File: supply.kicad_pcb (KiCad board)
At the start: 2 copper layers, 70 x 54.5 mm, 27 parts, among them J1 out, J2 2, J3 3, J4 1, J5 GND, J6 Conn_01x01_Female, J7 Conn_01x01_Female, J8 Conn_01x01_Female, J9 Conn_01x01_Female, U1 TPS61040DBV

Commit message: Add files via upload
updated
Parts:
- removed D3: SB140-E3/54, Diode_THT:D_DO-41_SOD81_P7.62mm_Horizontal
- added C10: 100nF, Capacitor_THT:C_Disc_D3.8mm_W2.6mm_P2.50mm, F.Cu at (94.5, 128.0)
- added C8: 10nF, Capacitor_THT:C_Disc_D3.8mm_W2.6mm_P2.50mm, F.Cu at (59.0, 120.5)
- added C9: 1nF, Capacitor_THT:C_Disc_D3.8mm_W2.6mm_P2.50mm, F.Cu at (95.0, 119.5)
- added R5: 118K, Resistor_THT:R_Axial_DIN0207_L6.3mm_D2.5mm_P7.62mm_Horizontal, F.Cu at (84.0, 123.5)
- added R6: 2.49K, Resistor_THT:R_Axial_DIN0207_L6.3mm_D2.5mm_P7.62mm_Horizontal, F.Cu at (88.5, 131.1)
- added SW1: TE6-1A-DC-1-PB, Connector_PinHeader_2.00mm:PinHeader_2x01_P2.00mm_Vertical, F.Cu at (47.5, 122.5)
- BT1: value Battery 9V -> ACC-9VCLIP-233M
- C1: value 4.7 uF -> 4.7uF; footprint Capacitor_THT:C_Disc_D3.0mm_W1.6mm_P2.50mm -> Capacitor_THT:C_Disc_D3.8mm_W2.6mm_P2.50mm
- C2: value 1uF -> 100nF; footprint Capacitor_THT:C_Disc_D3.0mm_W1.6mm_P2.50mm -> Capacitor_THT:C_Disc_D3.8mm_W2.6mm_P2.50mm
- C3: value 4.7 uF -> 1nF; footprint Capacitor_THT:C_Disc_D3.0mm_W1.6mm_P2.50mm -> Capacitor_THT:C_Disc_D3.8mm_W2.6mm_P2.50mm
- C4: value 4.7 uF -> 68nF; footprint Capacitor_THT:C_Disc_D3.0mm_W1.6mm_P2.50mm -> Capacitor_THT:C_Disc_D3.8mm_W2.6mm_P2.50mm
- C5, C6: footprint Capacitor_THT:C_Disc_D3.0mm_W1.6mm_P2.50mm -> Capacitor_THT:C_Disc_D3.8mm_W2.6mm_P2.50mm
- C7: value 250pF -> 300pF; footprint Capacitor_THT:C_Disc_D3.0mm_W1.6mm_P2.50mm -> Capacitor_THT:C_Disc_D3.8mm_W2.6mm_P2.50mm
- D1: value SB140-E3/54 -> BAT42; footprint Diode_THT:D_DO-41_SOD81_P7.62mm_Horizontal -> Diode_THT:D_DO-35_SOD27_P7.62mm_Horizontal
- D2: value SB140-E3/54 -> 656320A304F; footprint Diode_THT:D_DO-41_SOD81_P7.62mm_Horizontal -> LED_THT:LED_Rectangular_W3.0mm_H2.0mm
- J1: value out -> MJ-3536
- L1: value 22 uH -> 2.7uH; footprint Resistor_THT:R_Axial_DIN0207_L6.3mm_D2.5mm_P7.62mm_Horizontal -> Inductor_THT:L_Axial_L9.5mm_D4.0mm_P12.70mm_Horizontal_Fastron_SMCC
- R1: value 1M -> 9.53K
- R2: value 27K -> 1.18K
- U1: value TPS61040DBV -> LM5157; footprint Package_TO_SOT_SMD:SOT-23-5 -> Teensy:WQFN-16_EP_3.15x3.15_Pitch0.5mm
- moved C7 46.6 mm to (59.0, 117.5), turned to 90 degrees
- moved C4 43.3 mm to (52.5, 128.0), turned to 90 degrees
- moved C2 30.0 mm to (52.5, 123.0), turned to 90 degrees
- moved R2 22.0 mm to (82.9, 114.5), turned to 0 degrees
- moved D1 19.4 mm to (67.9, 114.0), turned to 0 degrees
- moved D2 17.4 mm to (101.5, 126.5), turned to 90 degrees
- moved R1 16.6 mm to (83.0, 119.5), turned to 0 degrees
- moved C1 13.6 mm to (52.5, 115.0)
- moved BT1 12.0 mm to (47.5, 115.0)
- moved C3 7.62 mm to (95.0, 114.5), turned to 0 degrees
- moved L1 4.02 mm to (65.3, 121.3)
- moved U1 3.47 mm to (71.4, 127.9)
- moved J1 1.12 mm to (47.8, 96.7)
- moved J5 1.12 mm to (47.8, 102.0)
- moved J6 0.50 mm to (45.5, 135.5)
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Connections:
- C2 pad 2: Net-(C2-Pad2) -> GND
- C4 pad 2: Net-(C3-Pad1) -> GND
- C7 pad 1: Net-(C4-Pad1) -> Net-(C7-Pad1)
- C7 pad 2: Net-(C7-Pad2) -> GND
- D1 pad 1: Net-(C3-Pad1) -> Net-(C10-Pad2)
- D1 pad 2: Net-(C2-Pad2) -> Net-(D1-Pad2)
- D2 pad 1: Net-(C2-Pad1) -> GND
- D2 pad 2: Net-(C3-Pad1) -> Net-(C10-Pad2)
- L1 pad 1: Net-(C2-Pad2) -> Net-(C2-Pad1)
- L1 pad 2: Net-(BT1-Pad1) -> Net-(D1-Pad2)
- R1 pad 1: Net-(C4-Pad1) -> Net-(R1-Pad1)
- R1 pad 2: Net-(C7-Pad2) -> GND
- R2 pad 1: Net-(C7-Pad2) -> Net-(C8-Pad2)
- R3 pad 1: Net-(C4-Pad1) -> Net-(C10-Pad2)
- R4 pad 2: Net-(C4-Pad1) -> Net-(C10-Pad2)
- U1 pad 1: Net-(C2-Pad2) -> GND
- U1 pad 2: GND -> Net-(C3-Pad1)
- U1 pad 3: Net-(C7-Pad2) -> Net-(C2-Pad1)
- U1 pad 4: Net-(BT1-Pad1) -> Net-(U1-Pad4)
- U1 pad 5: Net-(BT1-Pad1) -> Net-(R1-Pad1)
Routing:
- net Net-(C10-Pad2): track 0.00 -> 62.5 mm
- net Net-(C7-Pad1): track 0.00 -> 48.1 mm
- net Net-(C7-Pad2): track 41.0 -> 0.00 mm
- net Net-(R1-Pad1): track 0.00 -> 31.2 mm
- net Net-(C8-Pad2): track 0.00 -> 27.4 mm
- net Net-(C2-Pad1): track 24.5 -> 50.3 mm
- net Net-(C2-Pad2): track 25.6 -> 0.00 mm, vias 1 -> 0
- net Net-(D1-Pad2): track 0.00 -> 18.1 mm
- net Net-(R5-Pad2): track 0.00 -> 16.9 mm
- net GND: track 15.7 -> 3.68 mm
- net Net-(BT1-Pad1): track 24.3 -> 13.7 mm
- net Net-(C3-Pad1): track 22.1 -> 32.4 mm
- net Net-(C4-Pad1): track 59.0 -> 49.2 mm
- net Net-(J1-Pad1): track 6.07 -> 9.25 mm
- net Net-(C5-Pad1): track 29.2 -> 27.7 mm
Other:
- board text added: "AUDIO OUT"
- board text added: "PHANTOM POWER OUT"

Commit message: Add files via upload
Updated files.
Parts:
- added C11: 47uF, Capacitor_THT:C_Disc_D3.8mm_W2.6mm_P2.50mm, F.Cu at (52.0, 90.0)
- added R7: 100, Resistor_THT:R_Axial_DIN0207_L6.3mm_D2.5mm_P7.62mm_Horizontal, F.Cu at (54.0, 105.1)
- added RV1: R_POT_TRIM, Connector_PinHeader_2.54mm:PinHeader_1x03_P2.54mm_Vertical, F.Cu at (59.0, 91.0)
- added U2: NE5534, Package_DIP:DIP-8_W7.62mm_Socket, F.Cu at (58.4, 97.5)
- moved TR1 17.2 mm to (77.7, 101.0)
- moved C6 15.6 mm to (89.0, 107.5), turned to 270 degrees
- moved C5 15.0 mm to (89.0, 91.5), turned to 270 degrees
- moved R3 15.0 mm to (95.0, 102.0)
- moved R4 15.0 mm to (95.0, 91.0)
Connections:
- net Net-(C2-Pad1) renamed VCC
- J1 pad 1: Net-(J1-Pad1) -> GND
- J5 pad 1: GND -> Net-(J5-Pad1)
- TR1 pad 1: Net-(J1-Pad1) -> Net-(TR1-Pad1)
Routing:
- net Net-(J5-Pad1): track 0.00 -> 31.0 mm
- net Net-(C4-Pad1): track 49.2 -> 26.0 mm, vias 0 -> 1
- net VCC: track 50.3 -> 72.8 mm
- net Net-(TR1-Pad1): track 0.00 -> 16.7 mm
- net Net-(R7-Pad1): track 0.00 -> 16.6 mm
- net Net-(C6-Pad1): track 34.3 -> 18.8 mm
- net Net-(C5-Pad1): track 27.7 -> 12.9 mm
- net Net-(J1-Pad1): track 9.25 -> 0.00 mm
- net Net-(C10-Pad2): track 62.5 -> 71.1 mm
- net Net-(C11-Pad1): track 0.00 -> 8.33 mm
- net GND: track 3.68 -> 5.95 mm
- net Net-(C6-Pad2): track 4.05 -> 5.57 mm
- net Net-(C5-Pad2): track 4.55 -> 5.26 mm

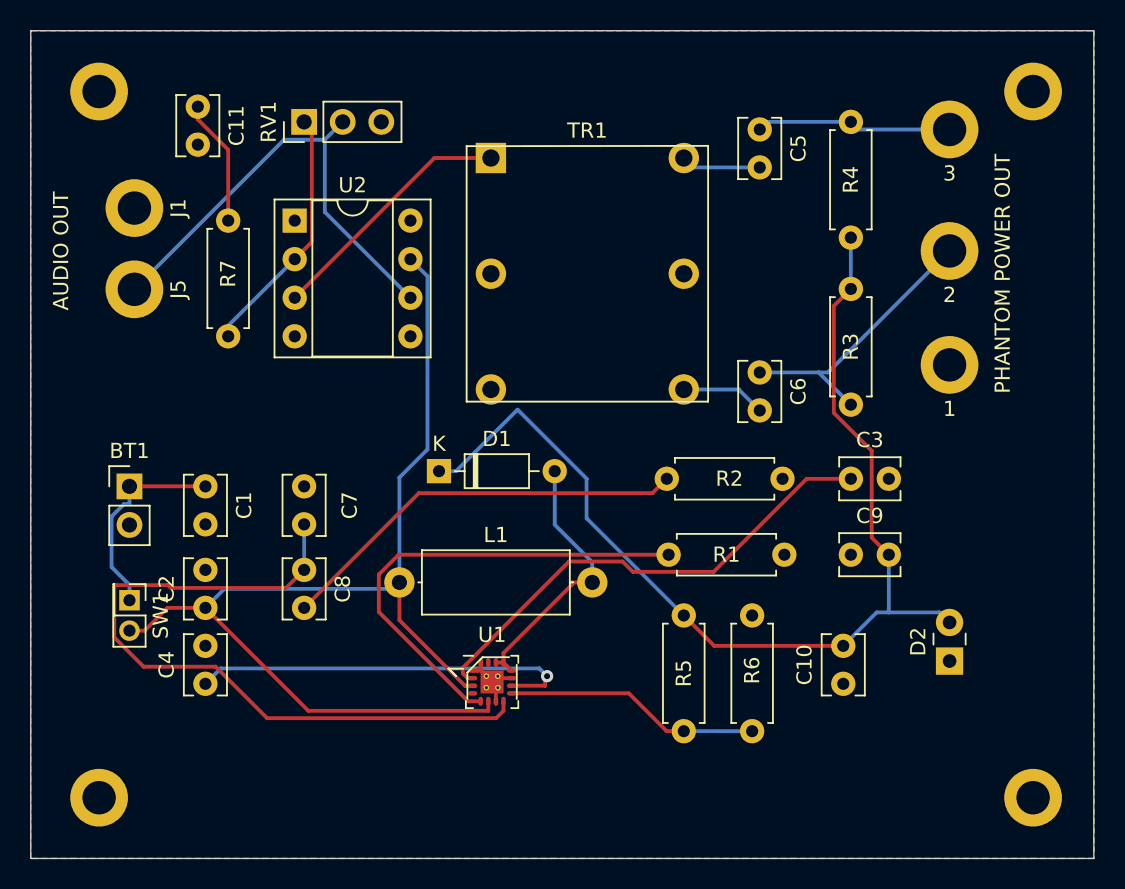
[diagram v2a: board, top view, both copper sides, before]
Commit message: Add files via upload
update, added correct diode and PCT fuse.
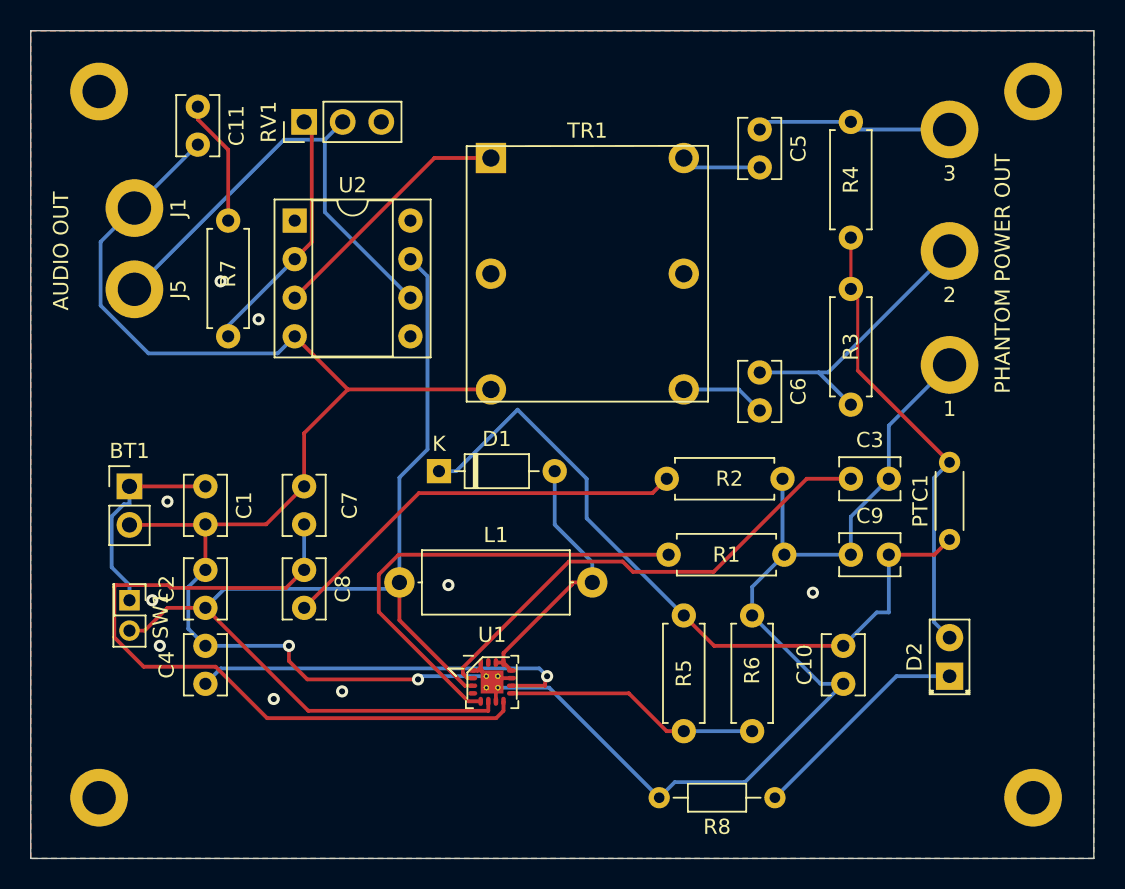
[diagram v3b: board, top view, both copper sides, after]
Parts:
- added PTC1: YPEL6250T, Resistor_THT:R_Axial_DIN0204_L3.6mm_D1.6mm_P5.08mm_Horizontal, F.Cu at (101.5, 118.5)
- added R8: 12K, Resistor_THT:R_Axial_DIN0204_L3.6mm_D1.6mm_P7.62mm_Horizontal, F.Cu at (90.0, 135.5)
- D1: value BAT42 -> BAT46
- D2: value 656320A304F -> 18-032.0055L; footprint LED_THT:LED_Rectangular_W3.0mm_H2.0mm -> LED_THT:LED_D2.0mm_W4.8mm_H2.5mm_FlatTop
- RV1: value R_POT_TRIM -> R_POT_TRIM-10K
- moved D2 1.00 mm to (101.5, 127.5)
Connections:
- D2 pad 1: GND -> Net-(D2-Pad1)
- D2 pad 2: Net-(C10-Pad2) -> Net-(D2-Pad2)
- J6 pad 1: Net-(J6-Pad1) -> Earth
- J7 pad 1: Net-(J7-Pad1) -> Earth
- J8 pad 1: Net-(J8-Pad1) -> Earth
- J9 pad 1: Net-(J9-Pad1) -> Earth
- R3 pad 1: Net-(C10-Pad2) -> Net-(D2-Pad2)
- R4 pad 2: Net-(C10-Pad2) -> Net-(D2-Pad2)
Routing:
- net GND: track 5.95 -> 166.4 mm, vias 0 -> 2
- net Net-(D2-Pad2): track 0.00 -> 30.4 mm
- net Net-(C10-Pad2): track 71.1 -> 48.4 mm
- net Net-(D2-Pad1): track 0.00 -> 14.8 mm
- net Earth: vias 0 -> 9
- added copper zone on B.Cu, net Earth
- added copper zone on F.Cu, net Earth
- removed copper zone on F.Cu, net (none)
- removed copper zone on B.Cu, net GND
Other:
- net class Default: clearance 0.2 -> 0.13; trace_width 0.25 -> 0.2
- rule trace_clearance: 0.2 -> 0.13

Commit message: Add files via upload
update due to component change.
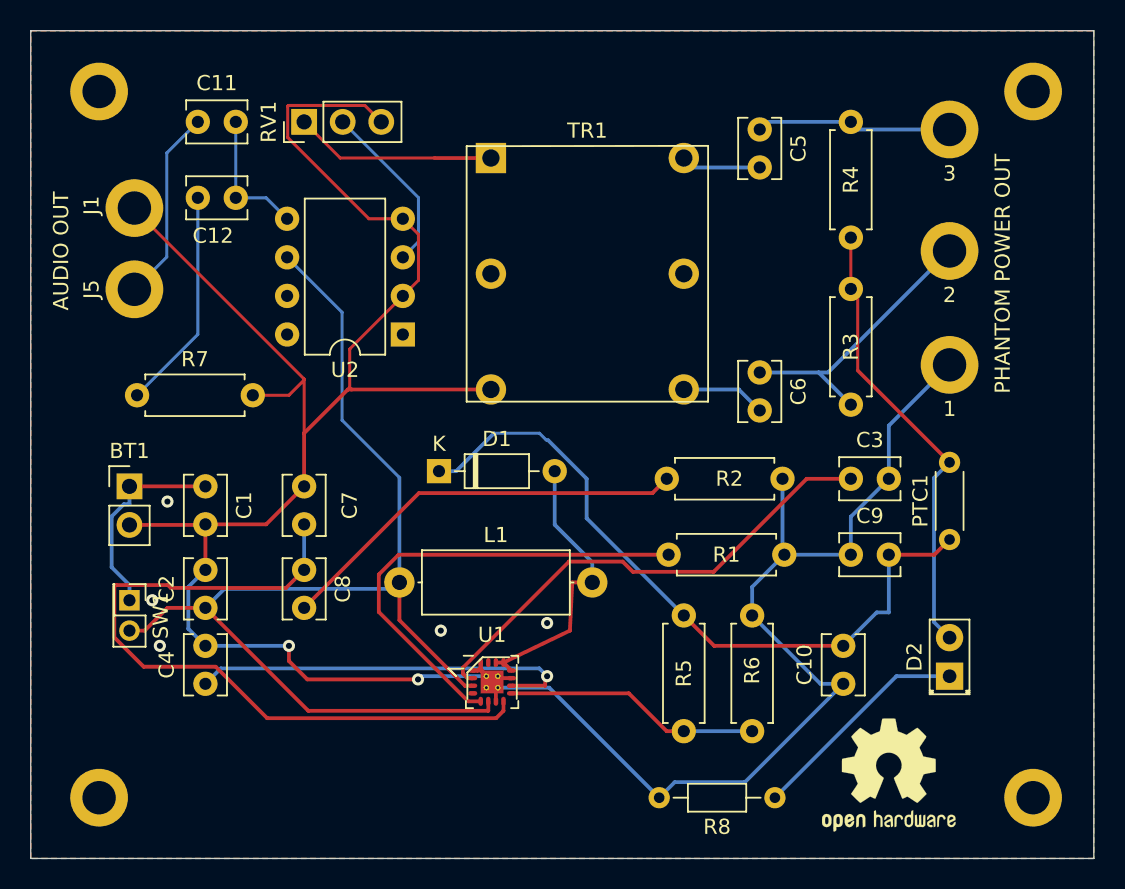
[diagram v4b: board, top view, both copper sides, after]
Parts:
- added C12: 0.05uF, Capacitor_THT:C_Disc_D3.8mm_W2.6mm_P2.50mm, F.Cu at (52.0, 96.0)
- added REF**: OSHW-Logo2_9.8x8mm_SilkScreen, Symbol:OSHW-Logo2_9.8x8mm_SilkScreen, F.Cu at (97.5, 134.0)
- C11: value 47uF -> 250uF
- U2: value NE5534 -> LM386; footprint Package_DIP:DIP-8_W7.62mm_Socket -> Package_DIP:DIP-8_W7.62mm
- moved U2 10.3 mm to (65.5, 105.0), turned to 180 degrees
- moved R7 7.15 mm to (48.0, 109.0), turned to 0 degrees
- moved C11 1.00 mm to (52.0, 91.0), turned to 0 degrees
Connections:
- C11 pad 2: GND -> Net-(C11-Pad2)
- J5 pad 1: Net-(J5-Pad1) -> Net-(C11-Pad1)
- R7 pad 1: Net-(R7-Pad1) -> Net-(C12-Pad1)
- R7 pad 2: Net-(C11-Pad1) -> GND
- RV1 pad 1: Net-(R7-Pad1) -> Net-(RV1-Pad1)
- RV1 pad 2: Net-(J5-Pad1) -> Net-(RV1-Pad2)
- RV1 pad 3: Net-(RV1-Pad3) -> GND
- TR1 pad 1: Net-(TR1-Pad1) -> Net-(RV1-Pad1)
- U2 pad 2: Net-(R7-Pad1) -> GND
- U2 pad 3: Net-(TR1-Pad1) -> Net-(RV1-Pad2)
- U2 pad 5: Net-(U2-Pad5) -> Net-(C11-Pad2)
- U2 pad 6: Net-(J5-Pad1) -> VCC
- U2 pad 7: VCC -> Net-(U2-Pad7)
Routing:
- net Net-(J5-Pad1): track 31.0 -> 0.00 mm
- net GND: track 166.4 -> 189.0 mm
- net Net-(TR1-Pad1): track 16.7 -> 0.00 mm
- net Net-(R7-Pad1): track 16.6 -> 0.00 mm
- net Net-(C12-Pad1): track 0.00 -> 14.7 mm
- net Net-(RV1-Pad1): track 0.00 -> 14.0 mm
- net Net-(RV1-Pad2): track 0.00 -> 11.4 mm
- net Net-(C11-Pad2): track 0.00 -> 8.95 mm
- net Net-(C11-Pad1): track 8.33 -> 12.8 mm
- net VCC: track 72.8 -> 74.7 mm
- net Net-(C10-Pad2): track 48.4 -> 47.1 mm
- net Net-(D1-Pad2): track 18.1 -> 18.9 mm
- net Earth: vias 9 -> 5

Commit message: Add files via upload
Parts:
- removed the REF** at (97.5, 134.0)
- removed TR1: 108F, supply:108F
- added REF**: OSHW-Logo2_14.6x12mm_SilkScreen, Symbol:OSHW-Logo2_14.6x12mm_SilkScreen, F.Cu at (77.0, 103.0)
- C11: value 250uF -> 10pF
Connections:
- C6 pad 2: Net-(C6-Pad2) -> GND
- RV1 pad 1: Net-(RV1-Pad1) -> Net-(C5-Pad2)
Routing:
- net Net-(C5-Pad2): track 5.26 -> 32.0 mm
- net Net-(RV1-Pad1): track 14.0 -> 0.00 mm
- net Net-(C6-Pad2): track 5.57 -> 0.00 mm
- net GND: track 189.0 -> 184.9 mm

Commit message: Add files via upload
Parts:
- removed C5, C6: 22nF, Capacitor_THT:C_Disc_D3.8mm_W2.6mm_P2.50mm
- removed R4: 6.81K, Resistor_THT:R_Axial_DIN0207_L6.3mm_D2.5mm_P7.62mm_Horizontal
- removed the REF** at (77.0, 103.0)
- added REF**: OSHW-Logo2_7.3x6mm_SilkScreen, Symbol:OSHW-Logo2_7.3x6mm_SilkScreen, F.Cu at (99.5, 134.5)
- added TR1: 108F, tastatur:108F, F.Cu at (77.2, 100.5)
- R3: value 6.81K -> 3.3K
- U2: value LM386 -> LM386N-4/NOPB
- moved R3 6.55 mm to (89.0, 104.6), turned to 90 degrees
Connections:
- J2 pad 1: Net-(C6-Pad1) -> /6
- J3 pad 1: Net-(C5-Pad1) -> /4
- R3 pad 2: Net-(C6-Pad1) -> /5
- RV1 pad 1: Net-(C5-Pad2) -> /1
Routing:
- net Net-(C5-Pad2): track 32.0 -> 0.00 mm
- net Net-(C4-Pad1): track 26.0 -> 57.8 mm, vias 1 -> 0
- net /4: track 0.00 -> 24.9 mm
- net /6: track 0.00 -> 20.7 mm
- net GND: track 184.9 -> 164.4 mm, vias 2 -> 0
- net Net-(C6-Pad1): track 18.8 -> 0.00 mm
- net Net-(C5-Pad1): track 12.9 -> 0.00 mm
- net /1: track 0.00 -> 12.7 mm
- net /5: track 0.00 -> 6.95 mm
- net Net-(C10-Pad2): track 47.1 -> 43.1 mm
- net VCC: track 74.7 -> 72.4 mm
- net Net-(C7-Pad1): track 48.1 -> 46.1 mm
- net Net-(D2-Pad2): track 30.4 -> 28.5 mm
- net Net-(RV1-Pad2): track 11.4 -> 10.6 mm

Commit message: Add files via upload
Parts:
- added C5: 100uF, Capacitor_THT:C_Disc_D3.8mm_W2.6mm_P2.50mm, F.Cu at (52.0, 132.0)
- added C6: 0.1uF, Capacitor_THT:C_Disc_D3.8mm_W2.6mm_P2.50mm, F.Cu at (59.0, 126.0)
- C11: value 10pF -> 220 µF; footprint Capacitor_THT:C_Disc_D3.8mm_W2.6mm_P2.50mm -> Capacitor_THT:CP_Radial_D6.3mm_P2.50mm
- D1: value BAT46 -> SB130-T
- R7: value 100 -> 10
- moved C11 11.5 mm to (52.5, 102.5)
- moved R7 10.9 mm to (58.9, 109.0)
- moved C12 5.10 mm to (51.0, 91.0)
- moved PTC1 4.53 mm to (102.0, 114.0), turned to 270 degrees
- moved R3 3.02 mm to (92.0, 105.0)
- moved TR1 2.00 mm to (79.2, 100.5)
- moved U2 1.12 mm to (66.6, 105.0)
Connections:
- D2 pad 2: Net-(D2-Pad2) -> Net-(C10-Pad2)
- PTC1 pad 1: Net-(C10-Pad2) -> Net-(PTC1-Pad1)
- PTC1 pad 2: Net-(D2-Pad2) -> Net-(C10-Pad2)
- R3 pad 1: Net-(D2-Pad2) -> Net-(PTC1-Pad1)
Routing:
- net Net-(C10-Pad2): track 43.1 -> 76.5 mm
- net Net-(D2-Pad2): track 28.5 -> 0.00 mm
- net Net-(PTC1-Pad1): track 0.00 -> 13.7 mm
- net GND: track 164.4 -> 176.6 mm
- net Net-(C11-Pad1): track 12.8 -> 4.87 mm
- net Net-(C12-Pad1): track 14.7 -> 21.3 mm
- net Net-(C11-Pad2): track 8.95 -> 15.5 mm
- net /6: track 20.7 -> 18.7 mm
- net /1: track 12.7 -> 14.7 mm
- net VCC: track 72.4 -> 74.1 mm
- net /4: track 24.9 -> 23.2 mm
- net /5: track 6.95 -> 7.79 mm
- net Earth: vias 5 -> 4

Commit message: Add files via upload
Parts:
- C5: footprint Capacitor_THT:C_Disc_D3.8mm_W2.6mm_P2.50mm -> Capacitor_THT:CP_Radial_D8.0mm_P3.50mm
- moved C5 3.35 mm to (55.0, 133.5), turned to 180 degrees
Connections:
- C5 pad 1: GND -> Net-(C10-Pad2)
- C5 pad 2: Net-(C10-Pad2) -> GND
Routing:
- net GND: track 176.6 -> 178.3 mm
- net Net-(C10-Pad2): track 76.5 -> 77.2 mm
